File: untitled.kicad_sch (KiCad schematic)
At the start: 9 parts, among them J20 Conn_01x04_Socket, J21 Conn_01x02_Socket, U17 LTV-247

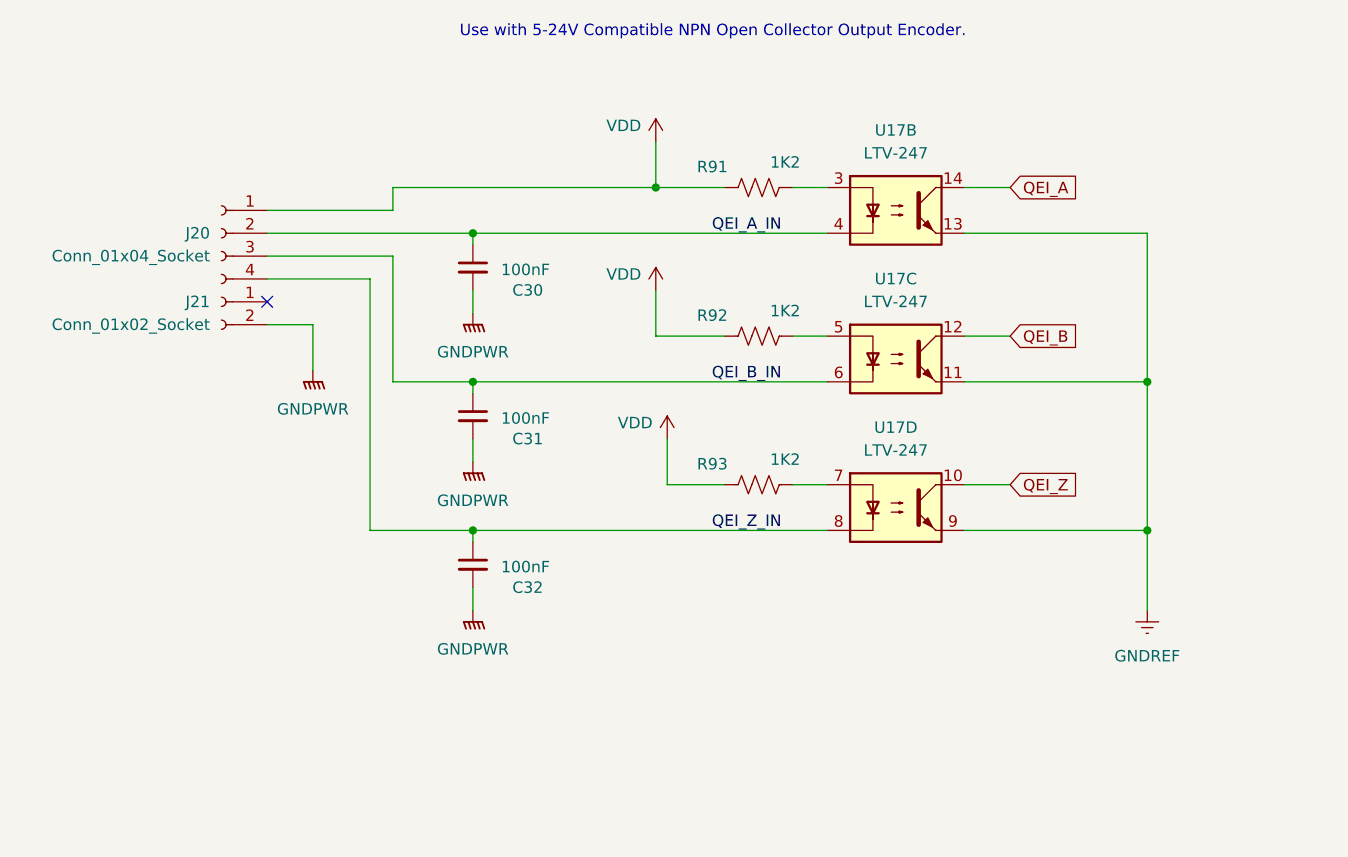
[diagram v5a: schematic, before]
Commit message: Updates to readme, working through testing and validation of board. Corrected pull ups on differential stepper outputs. Slight tweak to encoder. Tidied up some traces. Somehow lost the mounting holes and need to remember to put them back
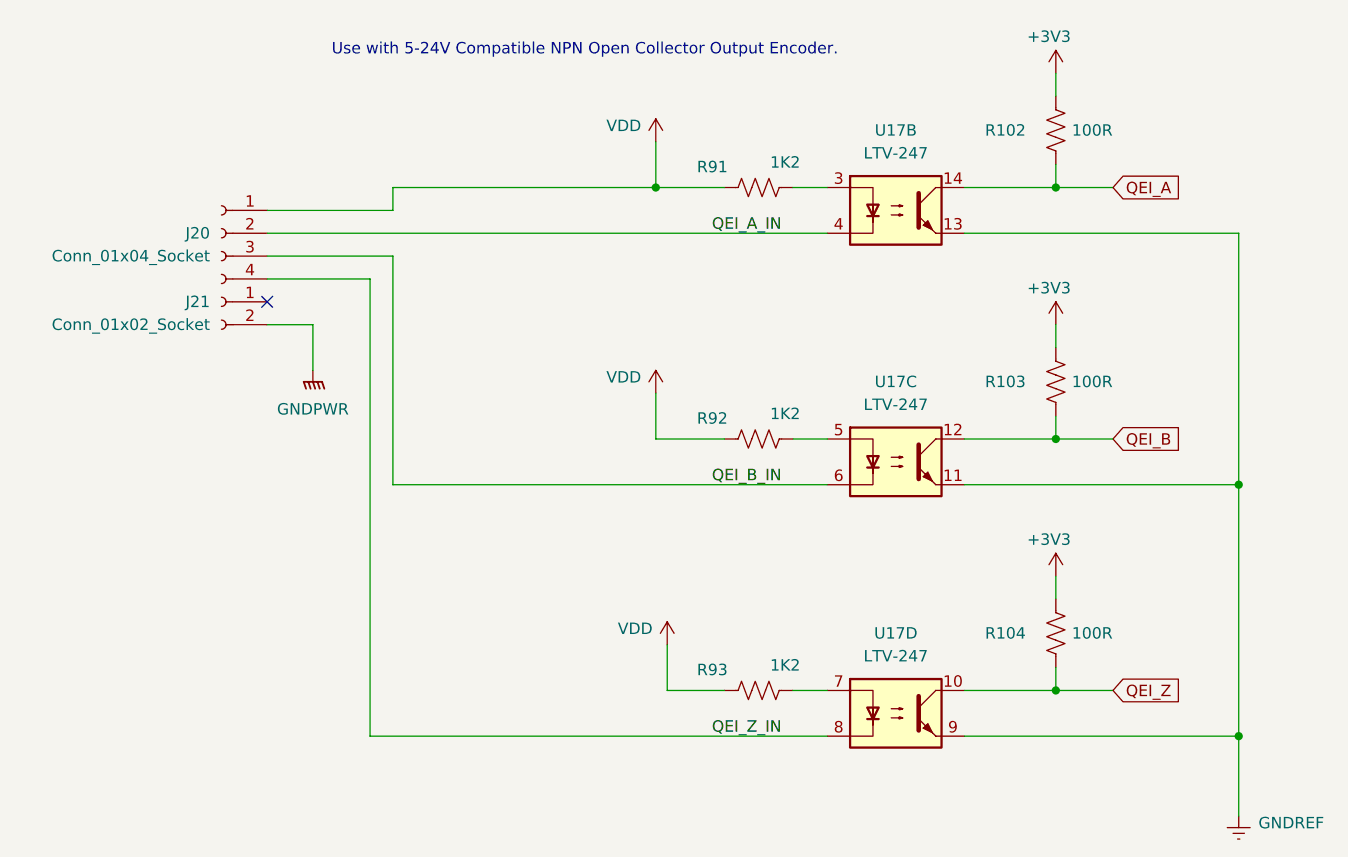
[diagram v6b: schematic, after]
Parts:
- removed C30, C31, C32: 100nF, Capacitor_SMD:C_1206_3216Metric_Pad1.33x1.80mm_HandSolder, symbol Device:C_Small
- added R102, R103, R104: 100R, Resistor_SMD:R_1206_3216Metric_Pad1.30x1.75mm_HandSolder, symbol Device:R_US
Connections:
- net QEI_A: now also R102.2
- net QEI_B: now also R103.2
- net QEI_Z: now also R104.2
- new net +3V3: R102.1, R103.1, R104.1
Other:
- moved on the sheet: R92, R93, U17C, U17D
